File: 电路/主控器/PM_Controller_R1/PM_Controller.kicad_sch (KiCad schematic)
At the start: 134 parts, among them J1 Conn_01x04_Socket, J10 Conn_02x04_Odd_Even, J11 Conn_02x06_Odd_Even, J2 Conn_01x04_Socket, J3 Conn_01x04_Socket, J4 Conn_01x04_Socket, J5 Conn_01x02_Pin, J6 Conn_01x02_Pin, J7 Conn_02x04_Odd_Even, J8 Conn_01x04_Pin, J9 Conn_01x04_Socket, P2V5 SolderJumper_2_Open, P3V3 SolderJumper_2_Open, Q1 AO3401A, Q2 AO3400A, Q3 AO3400A, Q4 AO3400A, Q5 AO3400A, Q6 AO3400A, U1 AT24CS08-SSHM, U10 TMP102xxDRL, U11 TPS2552DDBVR, U12 TLP127, U2 AMS1117-3.3, U3 STM32G431RBTx, U4 TPS61085DGK, U5 BQ21040DBV, U6 TPS2552DDBVR, U7 STM32L011D4Px, U8 ME6211C25M5, U9 AT24CS08-SSHM, Y1 32.768kHz, Y2 24Mhz

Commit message: Rev1.0版本可正常工作
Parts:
- added C39, C41: 100nf, Capacitor_SMD:C_0603_1608Metric_Pad1.08x0.95mm_HandSolder, symbol Device:C
- added C40: 22uf, Capacitor_Tantalum_SMD:CP_EIA-3528-21_Kemet-B_HandSolder, symbol Device:C_Polarized
- added R43: 22k, Resistor_SMD:R_0603_1608Metric_Pad0.98x0.95mm_HandSolder, symbol Device:R
- added R44: 100k, Resistor_SMD:R_0603_1608Metric_Pad0.98x0.95mm_HandSolder, symbol Device:R
- added U13: TPS2552DDBVR, DBV0006A_TEX, symbol TPS2552d:TPS2552DDBVR
- added U14: ADUM3201ARZ-RL7, ADUM3201:R_8_ADI, symbol ADUM3201:ADUM3201ARZ-RL7
- R42: value 100k -> 1k
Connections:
- net +3.3V: now also C39.1, C41.1, R44.1, U13.1 (IN), U14.1 (VDD1); no longer J8.1 (Pin_1)
- net GND: now also C39.2, C40.2, C41.2, R43.2, U13.2 (GND), U14.4 (GND1), U14.5 (GND2)
- net RX2: now also U14.2 (VOA); no longer J8.3 (Pin_3)
- net TX2: now also U14.3 (VIB); no longer J8.2 (Pin_2)
- net SDM_EN: now reaches U3.10 (PC2)
- net SDM_EN: now also R44.2, U13.3 (#EN)
- new net: R43.1, U13.5 (ILIM)
- new net LASER_3.3V: C40.1, J8.1 (Pin_1), U13.6 (OUT), U14.8 (VDD2)
- new net RX2_o: J8.3 (Pin_3), U14.7 (VIA)
- new net TX2_o: J8.2 (Pin_2), U14.6 (VOB)
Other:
- note added: "SDM18接口"
- moved on the sheet: BT1, C1, C2, C25, C26, C27, C28, C29, C3, C30, C31, C32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

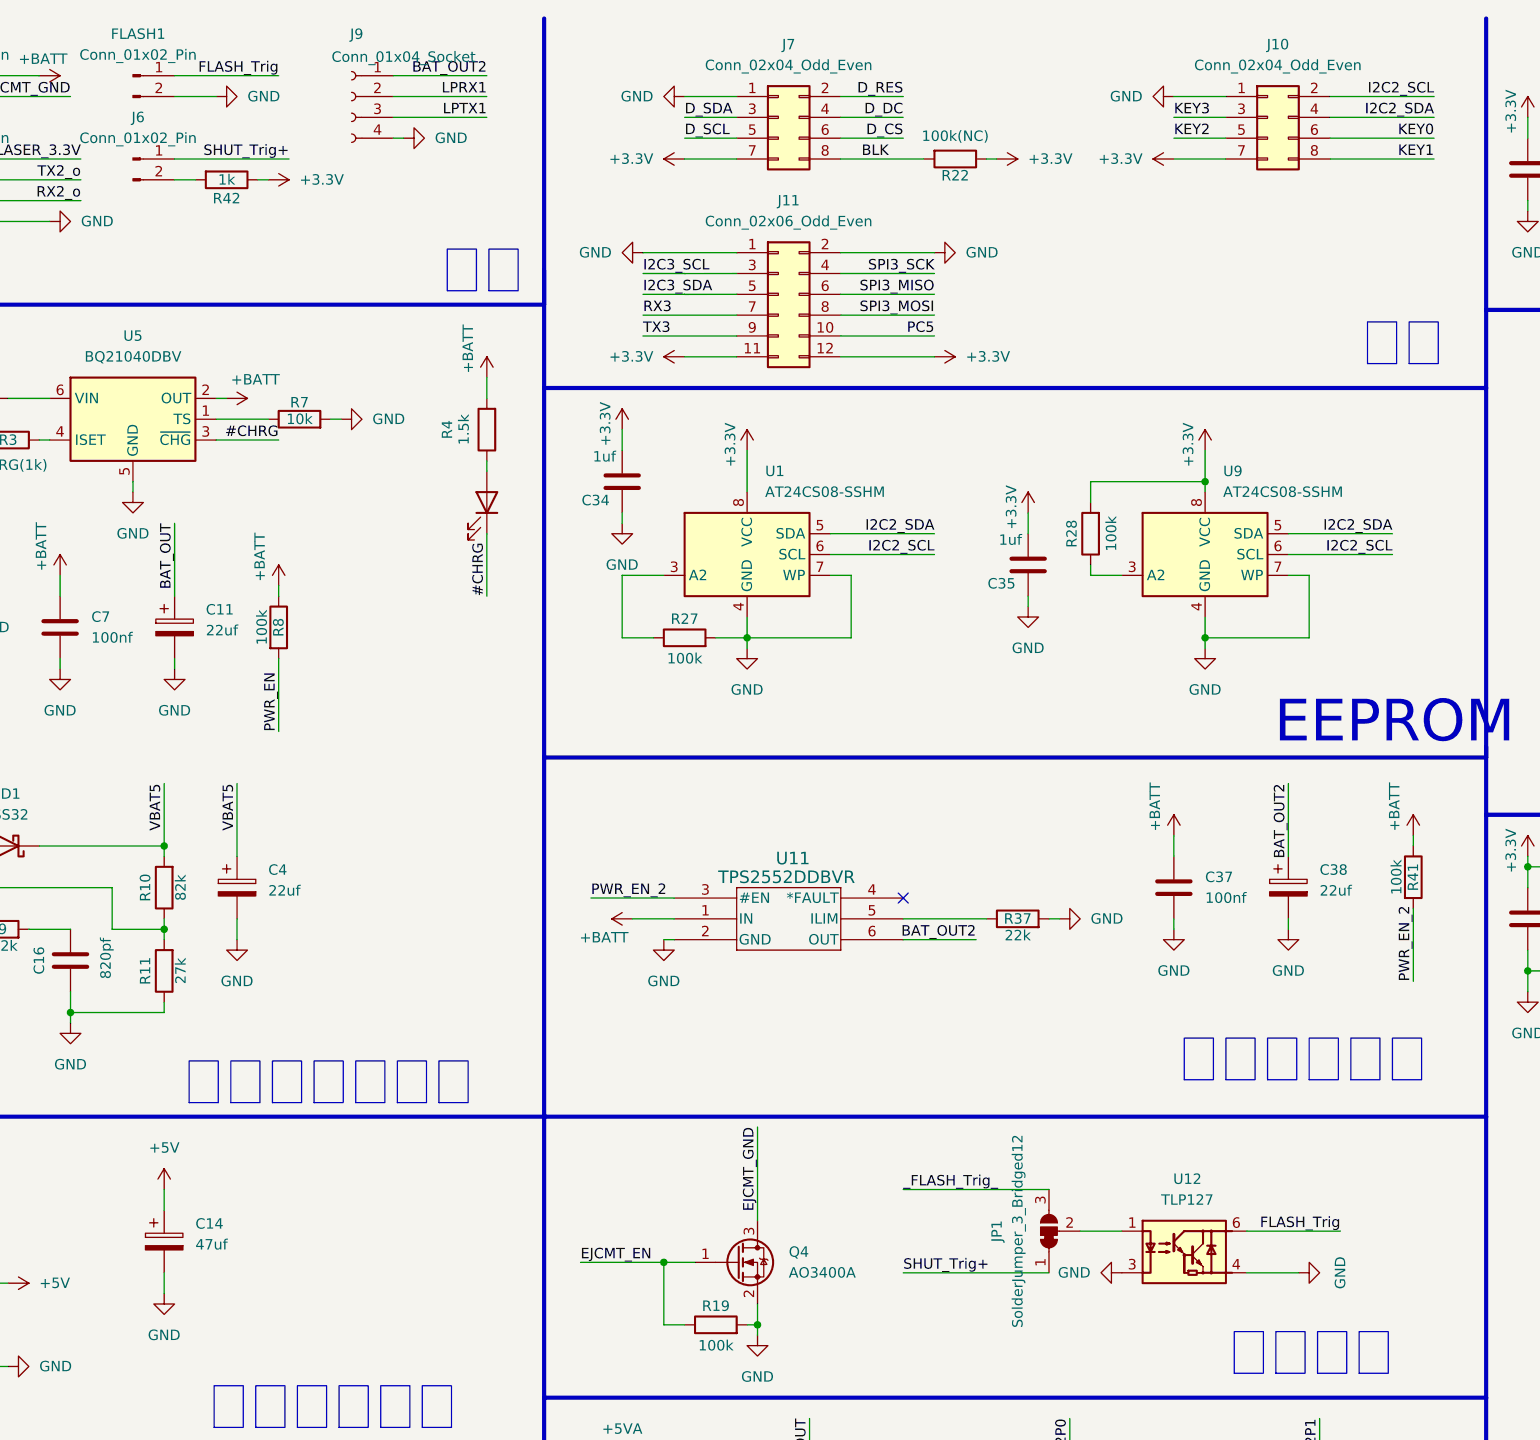
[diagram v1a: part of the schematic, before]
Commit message: 闪关灯功能OK 准备给电机加一个斜坡
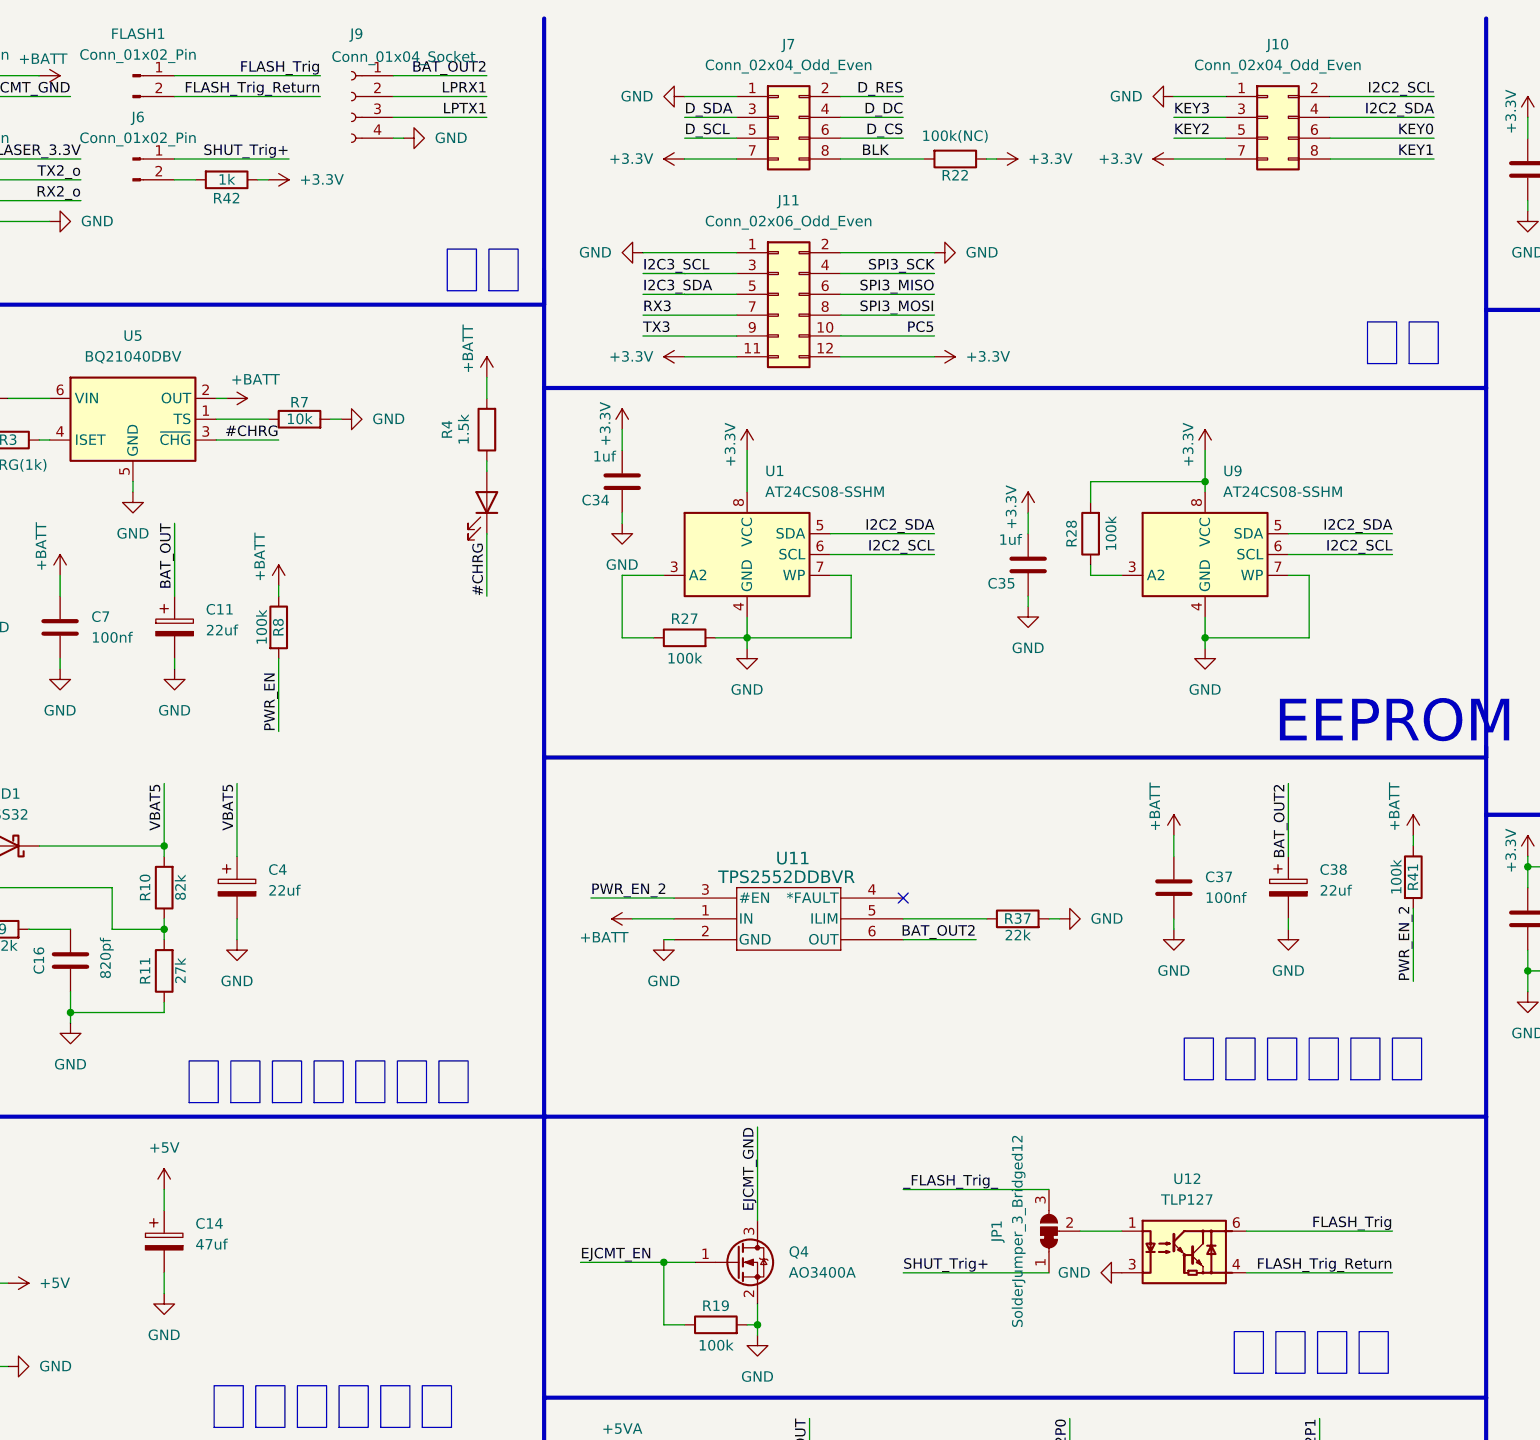
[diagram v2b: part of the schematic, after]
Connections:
- net GND: no longer FLASH1.2 (Pin_2), U12.4
- new net FLASH_Trig_Return: FLASH1.2 (Pin_2), U12.4
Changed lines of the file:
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@@
 	(wire
 		(pts
-			(xy 107.95 21.59) (xy 102.87 21.59)
+			(xy 102.87 21.59) (xy 120.65 21.59)
 		)
 		(stroke
@@
 	(wire
 		(pts
-			(xy 102.87 19.05) (xy 115.57 19.05)
+			(xy 102.87 19.05) (xy 120.65 19.05)
 		)
 		(stroke
@@
 	(wire
 		(pts
-			(xy 245.11 160.02) (xy 233.68 160.02)
+			(xy 251.46 160.02) (xy 233.68 160.02)
 		)
 		(stroke
@@
 	(wire
 		(pts
-			(xy 233.68 165.1) (xy 240.03 165.1)
+			(xy 233.68 165.1) (xy 251.46 165.1)
 		)
 		(stroke
@@
 	)
 	(label "FLASH_Trig"
-		(at 115.57 19.05 180)
+		(at 120.65 19.05 180)
 		(effects
 			(font
@@
 		)
 	)
+	(label "FLASH_Trig_Return"
+		(at 251.46 165.1 180)
+		(effects
+			(font
+				(size 1.27 1.27)
+			)
+			(justify right bottom)
+		)
+	)
 	(label "I2C2_SCL"
 		(at 251.46 77.47 180)
@@
 	)
 	(label "FLASH_Trig"
-		(at 245.11 160.02 180)
+		(at 251.46 160.02 180)
 		(effects
 			(font
@@
 		)
 	)
+	(label "FLASH_Trig_Return"
+		(at 120.65 21.59 180)
+		(effects
+			(font
+				(size 1.27 1.27)
+			)
+			(justify right bottom)
+		)
+	)
 	(label "LSE-"
 		(at 311.15 219.71 0)
@@
 	(symbol
 		(lib_id "power:GND")
-		(at 107.95 21.59 90)
-		(unit 1)
-		(exclude_from_sim no)
-		(in_bom yes)
-		(on_board yes)
-		(dnp no)
-		(fields_autoplaced yes)
-		(property "Reference" "#PWR076"
-			(at 114.3 21.59 0)
-			(effects
-				(font
-					(size 1.27 1.27)
-				)
-				(hide yes)
-			)
-		)
-		(property "Value" "GND"
-			(at 111.76 21.5899 90)
-			(effects
-				(font
-					(size 1.27 1.27)
-				)
-				(justify right)
-			)
-		)
-		(property "Footprint" ""
-			(at 107.95 21.59 0)
-			(effects
-				(font
-					(size 1.27 1.27)
-				)
-				(hide yes)
-			)
-		)
-		(property "Datasheet" ""
-			(at 107.95 21.59 0)
-			(effects
-				(font
-					(size 1.27 1.27)
-				)
-				(hide yes)
-			)
-		)
-		(property "Description" "Power symbol creates a global label with name \"GND\" , ground"
-			(at 107.95 21.59 0)
-			(effects
-				(font
-					(size 1.27 1.27)
-				)
-				(hide yes)
-			)
-		)
-		(pin "1"
-		)
-		(instances
-			(project "PM_Controller"
-				(path "/7185bc4a-db7d-484e-8ff2-a58428806037"
-					(reference "#PWR076")
-					(unit 1)
-				)
-			)
-		)
-	)
-	(symbol
-		(lib_id "power:GND")
 		(at 238.76 123.19 0)
 		(unit 1)
@@
 					(unit 1)
 				)
-			)
-		)
-	)
-	(symbol
-		(lib_id "power:GND")
-		(at 240.03 165.1 90)
-		(unit 1)
-		(exclude_from_sim no)
-		(in_bom yes)
-		(on_board yes)
-		(dnp no)
-		(fields_autoplaced yes)
-		(property "Reference" "#PWR078"
-			(at 246.38 165.1 0)
-			(effects
-				(font
-					(size 1.27 1.27)
-				)
-				(hide yes)
-			)
-		)
-		(property "Value" "GND"
-			(at 245.11 165.1 0)
-			(effects
-				(font
-					(size 1.27 1.27)
-				)
-			)
-		)
-		(property "Footprint" ""
-			(at 240.03 165.1 0)
-			(effects
-				(font
-					(size 1.27 1.27)
-				)
-				(hide yes)
-			)
-		)
-		(property "Datasheet" ""
-			(at 240.03 165.1 0)
-			(effects
-				(font
-					(size 1.27 1.27)
-				)
-				(hide yes)
-			)
-		)
-		(property "Description" "Power symbol creates a global label with name \"GND\" , ground"
-			(at 240.03 165.1 0)
-			(effects
-				(font
-					(size 1.27 1.27)
-				)
-				(hide yes)
-			)
-		)
-		(pin "1"
-		)
-		(instances
-			(project "PM_Controller"
-				(path "/7185bc4a-db7d-484e-8ff2-a58428806037"
-					(reference "#PWR078")
-					(unit 1)
-				)
